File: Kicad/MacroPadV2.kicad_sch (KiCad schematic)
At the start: 26 parts, among them K1 KSW, K10 KSW, K11 KSW, K12 KSW, K2 KSW, K3 KSW, K4 KSW, K5 KSW, K6 KSW, K7 KSW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

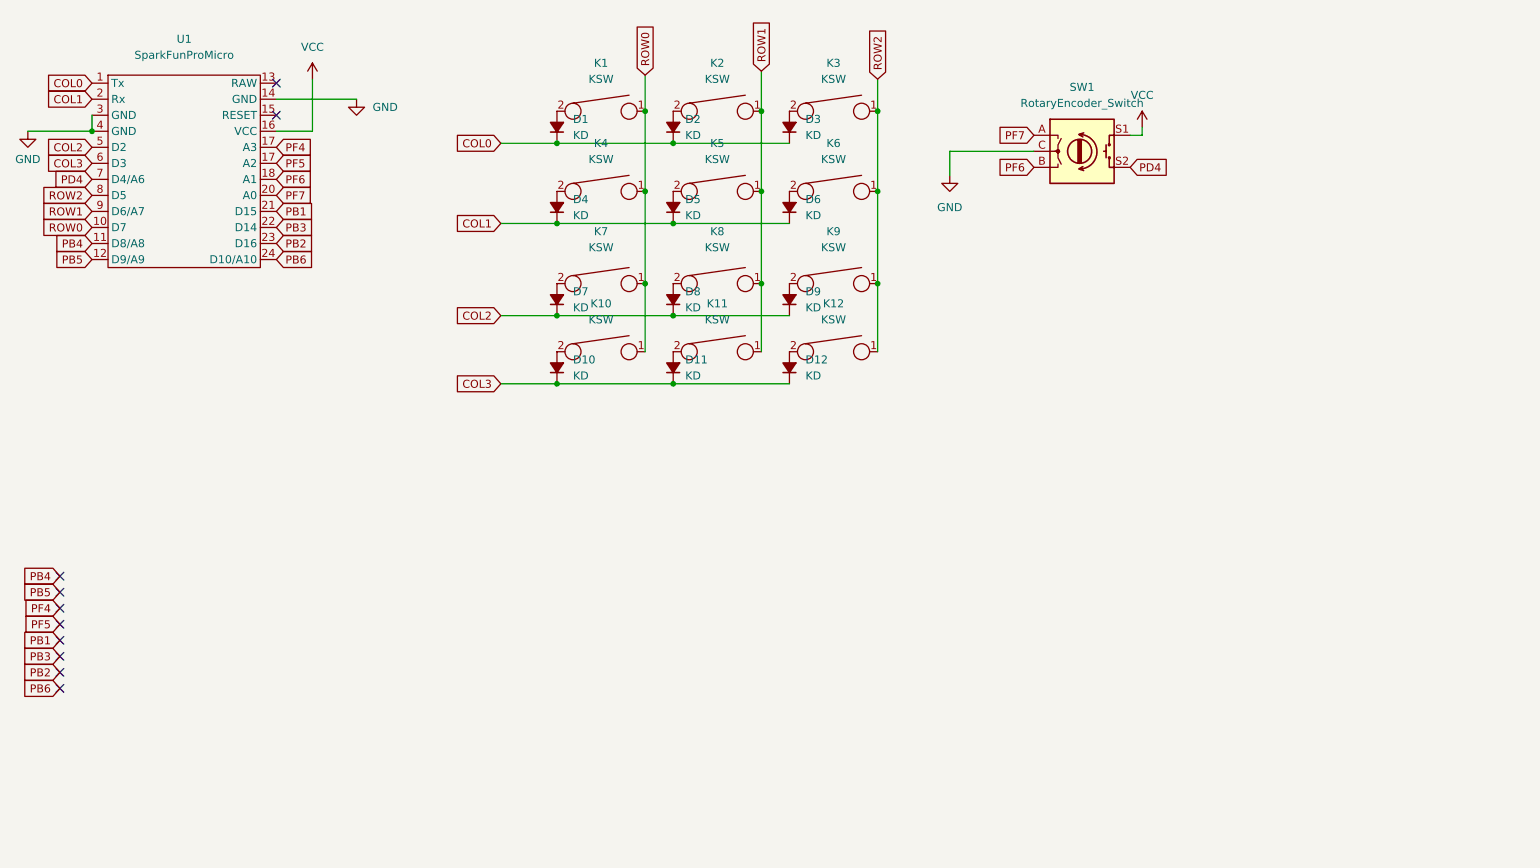
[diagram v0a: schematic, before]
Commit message: Temp Branch for storing work that will be merged to v2
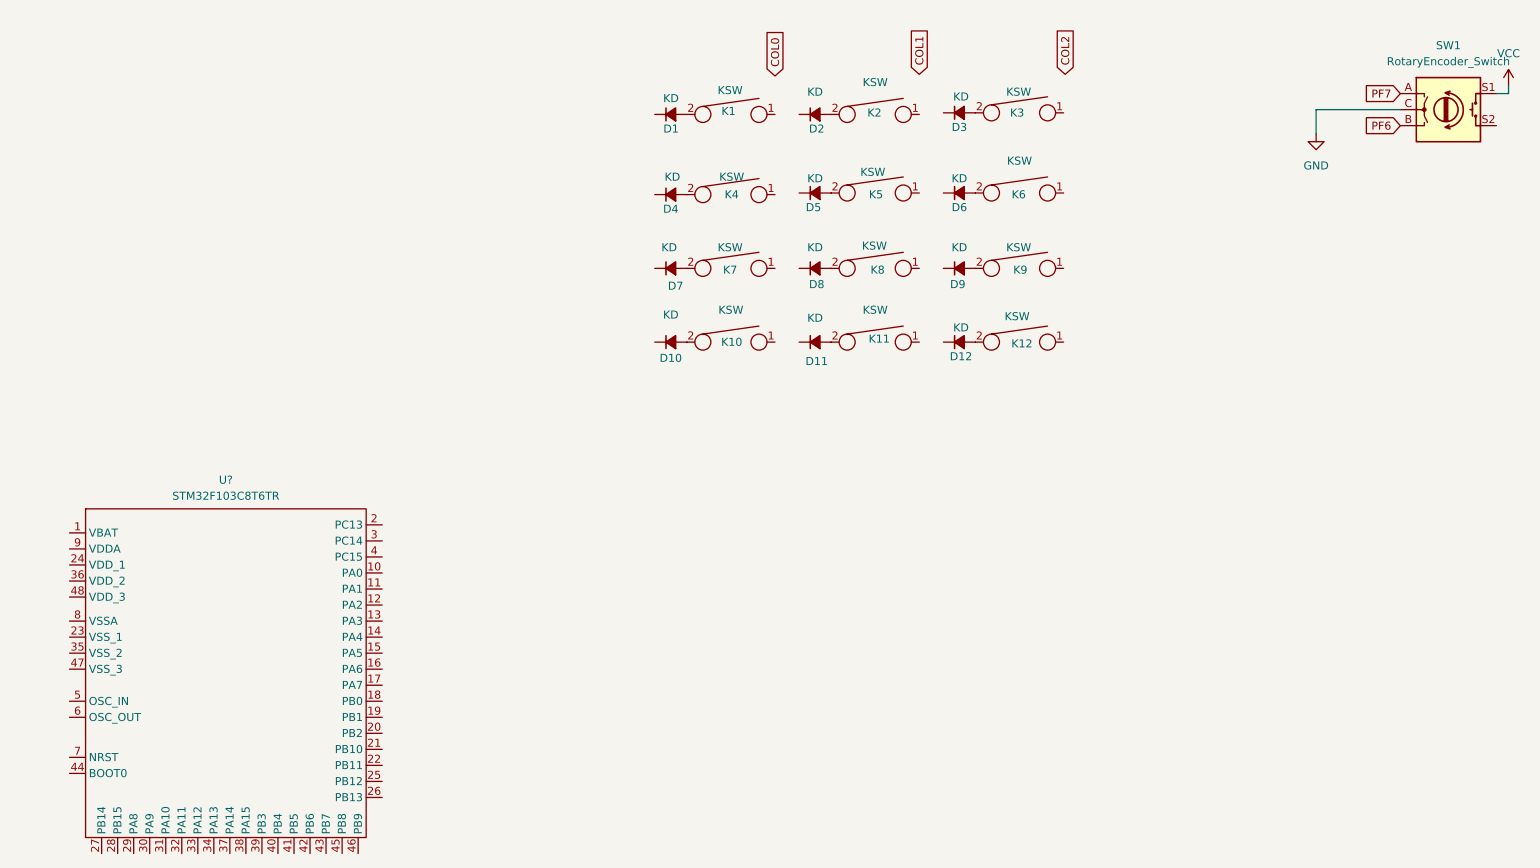
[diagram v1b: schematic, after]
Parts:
- removed U1: SparkFunProMicro, aarohanl:SparkFrunProMicro, symbol macropad_parts:SparkFunProMicro
- added U?: STM32F103C8T6TR, macrofp:LQFP48, symbol macropad_parts:STM32F103C8T6TR
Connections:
- net COL0: no longer D1.1 (K), D2.1 (K), D3.1 (K)
- net COL1: no longer D4.1 (K), D5.1 (K), D6.1 (K)
- net COL2: no longer D7.1 (K), D8.1 (K), D9.1 (K)
- removed net COL3: D10.1 (K), D11.1 (K), D12.1 (K)
- net PD4: no longer names the net of SW1.S2
- removed net ROW0: K1.1, K10.1, K4.1, K7.1
- removed net ROW1: K11.1, K2.1, K5.1, K8.1
- removed net ROW2: K12.1, K3.1, K6.1, K9.1
- no-connect marks 10 -> 0
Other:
- moved on the sheet: D1, D10, D11, D12, D2, D3, D4, D5, D6, D7, D8, D9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
